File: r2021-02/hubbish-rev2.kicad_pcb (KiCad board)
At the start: 4 copper layers, 103.6 x 71.8 mm, 100 parts, among them J1 Conn_01x06, J10 USB_A_DUAL, J4 USB_A (female down), J5 Conn_01x03_Male, J6 USB_A_DUAL, J7 USB_A_DUAL, J8 USB_A male UP, J9 USB_B_Micro (up), U1 2k i2c eeprom, U10 NUP4202, U11 NUP4202, U12 NUP4202, U13 NUP4202, U14 NUP4202, U15 NUP4202, U16 NUP4202, U17 NUP4202, U18 SY8366H, U2 SE5120ST33, U3 USB2517, U4 APL3511C, U5 APL3511C, U6 APL3511C, U7 APL3511C, U8 APL3511C, U9 APL3511C, Y1 24MHz

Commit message: start rev2
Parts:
- removed C31: 100uF, Capacitor_SMD:CP_Elec_5x5.4
- removed J10, J7: USB_A_DUAL, Connector_USB:USB_A_Wuerth_61400826021_Horizontal_Stacked
- added C36: 10uF/50V, Capacitor_SMD:C_0805_2012Metric, F.Cu at (118.9, 61.7)
- added C37: 2.2uF, Capacitor_SMD:C_0603_1608Metric, F.Cu at (132.0, 65.0)
- added C38: 100nF, Capacitor_SMD:C_0603_1608Metric, F.Cu at (139.0, 108.5)
- added C39: Cff, Capacitor_SMD:C_0603_1608Metric, F.Cu at (135.9, 119.0)
- added C40: 22uF/6.3V, Capacitor_SMD:C_0805_2012Metric, F.Cu at (116.5, 72.6)
- added C41: 22uF/6.3V, Capacitor_SMD:C_0805_2012Metric, F.Cu at (120.5, 66.1)
- added C42: 22uF/6.3V, Capacitor_SMD:C_0805_2012Metric, F.Cu at (112.0, 72.6)
- added C43: 100uF, Capacitor_SMD:CP_Elec_5x5.4, F.Cu at (86.4, 144.6)
- added D12: SMF24A, Diode_SMD:D_SOD-123F, F.Cu at (106.2, 77.0)
- added D13: MBR1040, Package_TO_SOT_SMD:TO-252-2_TabPin1, F.Cu at (90.4, 65.3)
- added J2: USB_A_Stacked, Connector_USB:USB_A_Wuerth_61400826021_Horizontal_Stacked, F.Cu at (154.4, 140.2)
- added J3: USB_A_Stacked, Connector_USB:USB_A_Wuerth_61400826021_Horizontal_Stacked, F.Cu at (126.6, 142.7)
- added L1: 2.2uH, Inductor_SMD:L_CHILISIN_BMRx00060630, F.Cu at (108.8, 66.0)
- added R23: Rff, Resistor_SMD:R_0603_1608Metric, F.Cu at (125.7, 71.4)
- added R24: 100k/1%, Resistor_SMD:R_0603_1608Metric, F.Cu at (121.1, 73.4)
- added R25: 13k6/1%, Resistor_SMD:R_0603_1608Metric, F.Cu at (120.8, 77.1)
- added U19: APL3511C, Package_TO_SOT_SMD:SOT-23-5, F.Cu at (168.7, 114.1)
- C1: value 100uF -> 1uF; footprint Capacitor_SMD:CP_Elec_5x5.4 -> Capacitor_SMD:C_0603_1608Metric
- D1: value SD05-7 -> DF2S6.2FS,L3M; footprint Diode_SMD:D_SOD-323 -> Diode_SMD:D_SOD-923
- D9: value D_Small -> SM400x; footprint Diode_SMD:D_SOD-323 -> Diode_SMD:D_SOD-123F
- J6: value USB_A_DUAL -> USB_A_Stacked
- JP1: value Jumper_NO_Small -> Jumper_2_Open; footprint Connector_PinHeader_2.54mm:PinHeader_1x02_P2.54mm_Vertical -> TestPoint:TestPoint_2Pads_Pitch2.54mm_Drill0.8mm
- moved R21 145.9 mm to (179.9, 180.0), turned to 0 degrees
- moved R19 106.9 mm to (202.1, 162.6), turned to 0 degrees
- moved R10 104.4 mm to (205.0, 155.7), turned to 0 degrees
- moved D10 96.4 mm to (196.8, 152.5)
- moved D11 92.9 mm to (170.5, 180.7), turned to 0 degrees
- moved R15 92.1 mm to (209.0, 155.7), turned to 0 degrees
- moved R6 88.0 mm to (118.7, 131.5), turned to 0 degrees
- moved H2 86.4 mm to (178.2, 59.3)
- moved R4 84.7 mm to (126.7, 130.9)
- moved D3 82.8 mm to (175.0, 79.0), turned to 0 degrees
- moved D2 82.7 mm to (175.3, 75.9), turned to 0 degrees
- moved R20 81.3 mm to (180.3, 172.9), turned to 0 degrees
- moved C33 76.9 mm to (131.9, 121.5)
- moved D8 76.9 mm to (180.7, 169.3)
- moved H1 73.2 mm to (178.2, 52.3)
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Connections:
- C19 pad 1: +5V -> /downstream-port-power/VBUS_DS
- J1 pad 6: (no net) -> Net-(D13-Pad2)
- J4 pad 1: +5V -> /downstream-port-power/VBUS_DS
- J5 pad 2: /upstream-config-leds/CFG_SEL0 -> /upstream-config-leds/EE_SCL
- J6 pad 1: /downstream-port-power/VBUS3 -> /downstream-port-power/VBUS5
- J6 pad 2: /downstream-port-power/U3- -> /downstream-port-power/U5-
- J6 pad 3: /downstream-port-power/U3+ -> /downstream-port-power/U5+
- J6 pad 5: /downstream-port-power/VBUS4 -> /downstream-port-power/VBUS6
- J6 pad 6: /downstream-port-power/U4- -> /downstream-port-power/U6-
- J6 pad 7: /downstream-port-power/U4+ -> /downstream-port-power/U6+
- R7 pad 2: /upstream-config-leds/CFG_SEL0 -> /upstream-config-leds/CFG_SEL0-EE_SCL
- R8 pad 1: /upstream-config-leds/CFG_SEL0 -> /upstream-config-leds/CFG_SEL0-EE_SCL
- U1 pad 6: /upstream-config-leds/CFG_SEL0 -> /upstream-config-leds/EE_SCL
- U10 pad 3: unconnected-(U10-Pad3) -> (no net)
- U10 pad 4: unconnected-(U10-Pad4) -> (no net)
- U11 pad 3: unconnected-(U11-Pad3) -> (no net)
- U11 pad 4: unconnected-(U11-Pad4) -> (no net)
- U12 pad 1: unconnected-(U12-Pad1) -> (no net)
- U12 pad 6: unconnected-(U12-Pad6) -> (no net)
- U13 pad 3: unconnected-(U13-Pad3) -> (no net)
- U13 pad 4: unconnected-(U13-Pad4) -> (no net)
- U14 pad 1: unconnected-(U14-Pad1) -> (no net)
- U14 pad 6: unconnected-(U14-Pad6) -> (no net)
- U15 pad 1: unconnected-(U15-Pad1) -> (no net)
- U15 pad 6: unconnected-(U15-Pad6) -> (no net)
- U16 pad 1: unconnected-(U16-Pad1) -> (no net)
- U16 pad 6: unconnected-(U16-Pad6) -> (no net)
- U17 pad 1: unconnected-(U17-Pad1) -> (no net)
- U17 pad 6: unconnected-(U17-Pad6) -> (no net)
- U18 pad 1: unconnected-(U18-Pad1) -> GND
- U18 pad 10: unconnected-(U18-Pad10) -> (no net)
- U18 pad 11: unconnected-(U18-Pad11) -> (no net)
- U18 pad 12: unconnected-(U18-Pad12) -> +VDC
- U18 pad 2: unconnected-(U18-Pad2) -> Net-(C38-Pad2)
- U18 pad 5: (no net) -> +VDC
- U18 pad 6: (no net) -> +VDC
- U18 pad 7: unconnected-(U18-Pad7) -> Net-(C38-Pad1)
- U18 pad 8: unconnected-(U18-Pad8) -> Net-(C37-Pad1)
- U18 pad 9: unconnected-(U18-Pad9) -> Net-(R23-Pad1)
- U3 pad 14: unconnected-(U3-Pad14) -> (no net)
- U3 pad 16: unconnected-(U3-Pad16) -> (no net)
- U3 pad 18: unconnected-(U3-Pad18) -> (no net)
- U3 pad 30: unconnected-(U3-Pad30) -> /downstream-port-power/EN_DS
- U3 pad 32: unconnected-(U3-Pad32) -> (no net)
- U3 pad 34: unconnected-(U3-Pad34) -> (no net)
- U3 pad 35: unconnected-(U3-Pad35) -> /downstream-port-power/OC_DS
- U3 pad 41: /upstream-config-leds/CFG_SEL0 -> /upstream-config-leds/CFG_SEL0-EE_SCL
- U3 pad 48: unconnected-(U3-Pad48) -> (no net)
- U3 pad 50: unconnected-(U3-Pad50) -> (no net)
- U3 pad 60: Net-(C4-Pad1) -> (no net)
- U3 pad 61: Net-(C5-Pad2) -> (no net)
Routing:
- net GNDPWR: track 306.4 -> 0.00 mm, vias 1 -> 0
- net +3V3: track 109.4 -> 0.00 mm, vias 27 -> 0
- net /upstream-config-leds/CFG_SEL1: track 98.5 -> 0.00 mm
- net /downstream-port-power/EN5: track 89.0 -> 0.00 mm, vias 2 -> 0
- net /downstream-port-power/OC5: track 87.8 -> 0.00 mm, vias 2 -> 0
- net /upstream-config-leds/UP-: track 85.4 -> 0.00 mm, vias 2 -> 0
- net /upstream-config-leds/UP+: track 84.4 -> 0.00 mm, vias 2 -> 0
- net GND: track 77.4 -> 0.00 mm, vias 59 -> 0
- net /upstream-config-leds/LED_A3: track 75.7 -> 0.00 mm, vias 2 -> 0
- net /upstream-config-leds/LED_A6: track 75.4 -> 0.00 mm, vias 2 -> 0
- net /downstream-port-power/EN6: track 73.6 -> 0.00 mm, vias 2 -> 0
- net /upstream-config-leds/LED_A1: track 72.6 -> 0.00 mm, vias 4 -> 0
- net /downstream-port-power/OC6: track 69.9 -> 0.00 mm, vias 2 -> 0
- net /upstream-config-leds/LED_A7: track 68.5 -> 0.00 mm, vias 2 -> 0
- net /downstream-port-power/EN3: track 67.5 -> 0.00 mm, vias 2 -> 0
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- removed copper zone on F.Cu, net +3V3
- removed copper zone on In2.Cu, net +3V3
- removed copper zone on In2.Cu, net +5V
- removed copper zone on B.Cu, net /upstream-config-leds/LED_DRIVE
- removed copper zone on F.Cu, net GND
- removed copper zone on In1.Cu, net GND
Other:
- board size 103.6 x 71.8 mm -> 100 x 100 mm
- copper layers 4 -> 2
- board text removed: "+5V"
- board text removed: "0"
- board text removed: "1"
- board text removed: "2"
- board text removed: "BIG fatto 30W 5V supply here one day y0"
- board text removed: "CFG_SEL"
- board text removed: "GND"
- board text removed: "GND SCL SDA"
- board text removed: "HI"
- board text removed: "HiSpeed"
- board text removed: "JLCJLCJLCJLC"
- board text removed: "JLCPCB 2313 stackup!"
- board text removed: "LO"
- board text removed: "Port 1/2"
- board text removed: "Port 3/4"
- board text removed: "Port 5"
- board text removed: "Port 6/7"
- board text removed: "Port LEDs Green: LS Red: FS Orange: HS"
- board text removed: "Reset"
- board text removed: "Upstream"
- board text removed: "github.com/karlp/hubbish rev 2020-03"

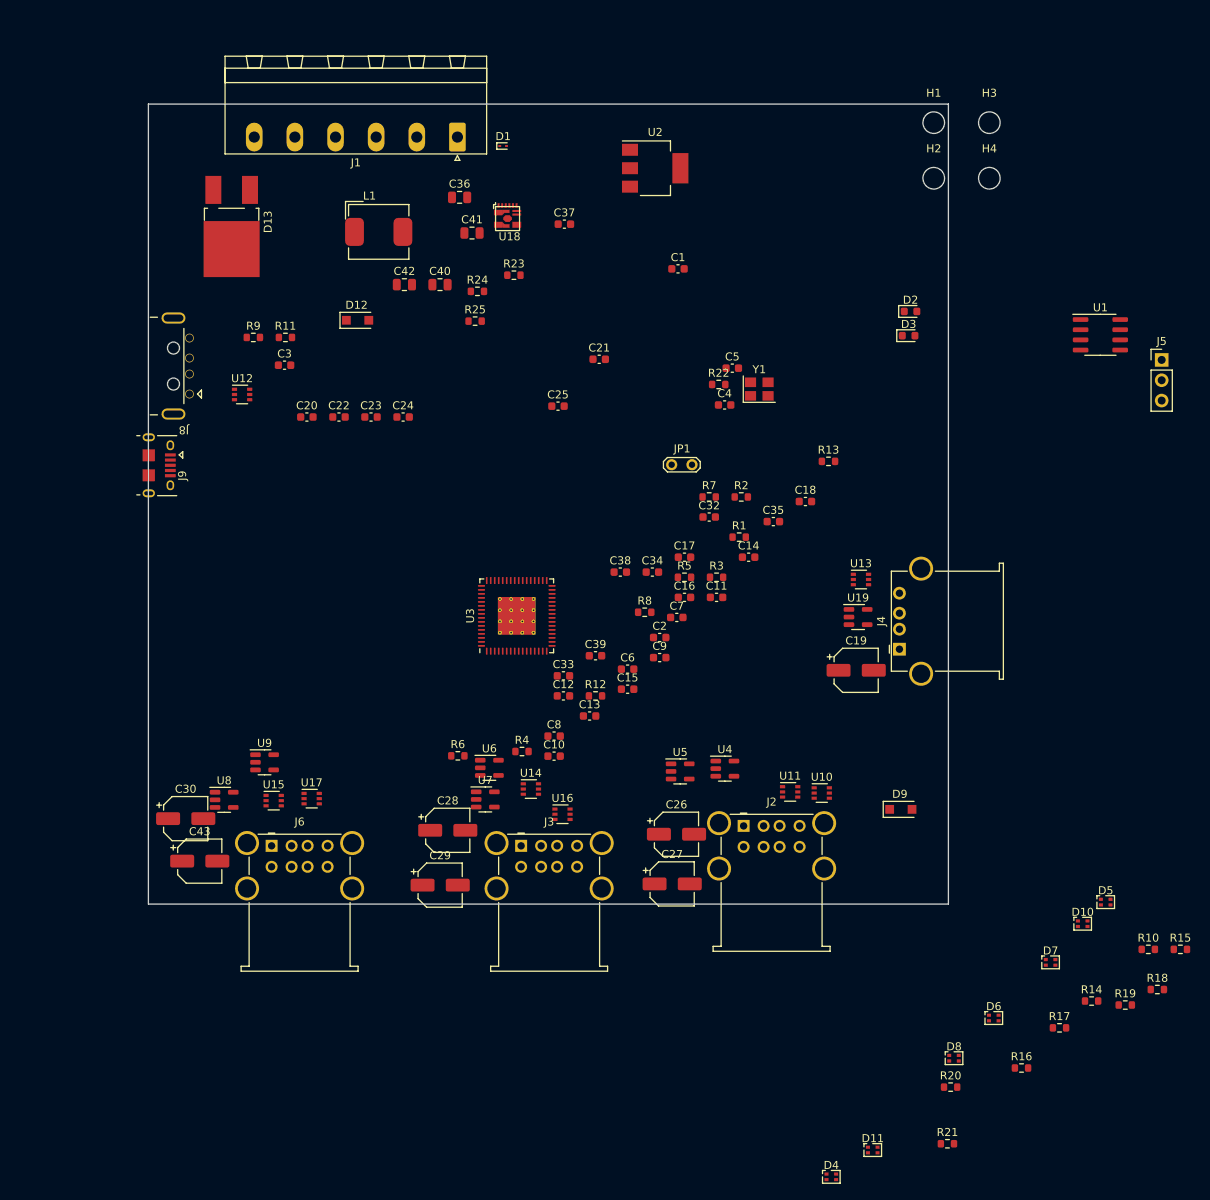
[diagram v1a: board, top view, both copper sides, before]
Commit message: rev2: start pcb work.
Looks like lots of space on a 100mm square...
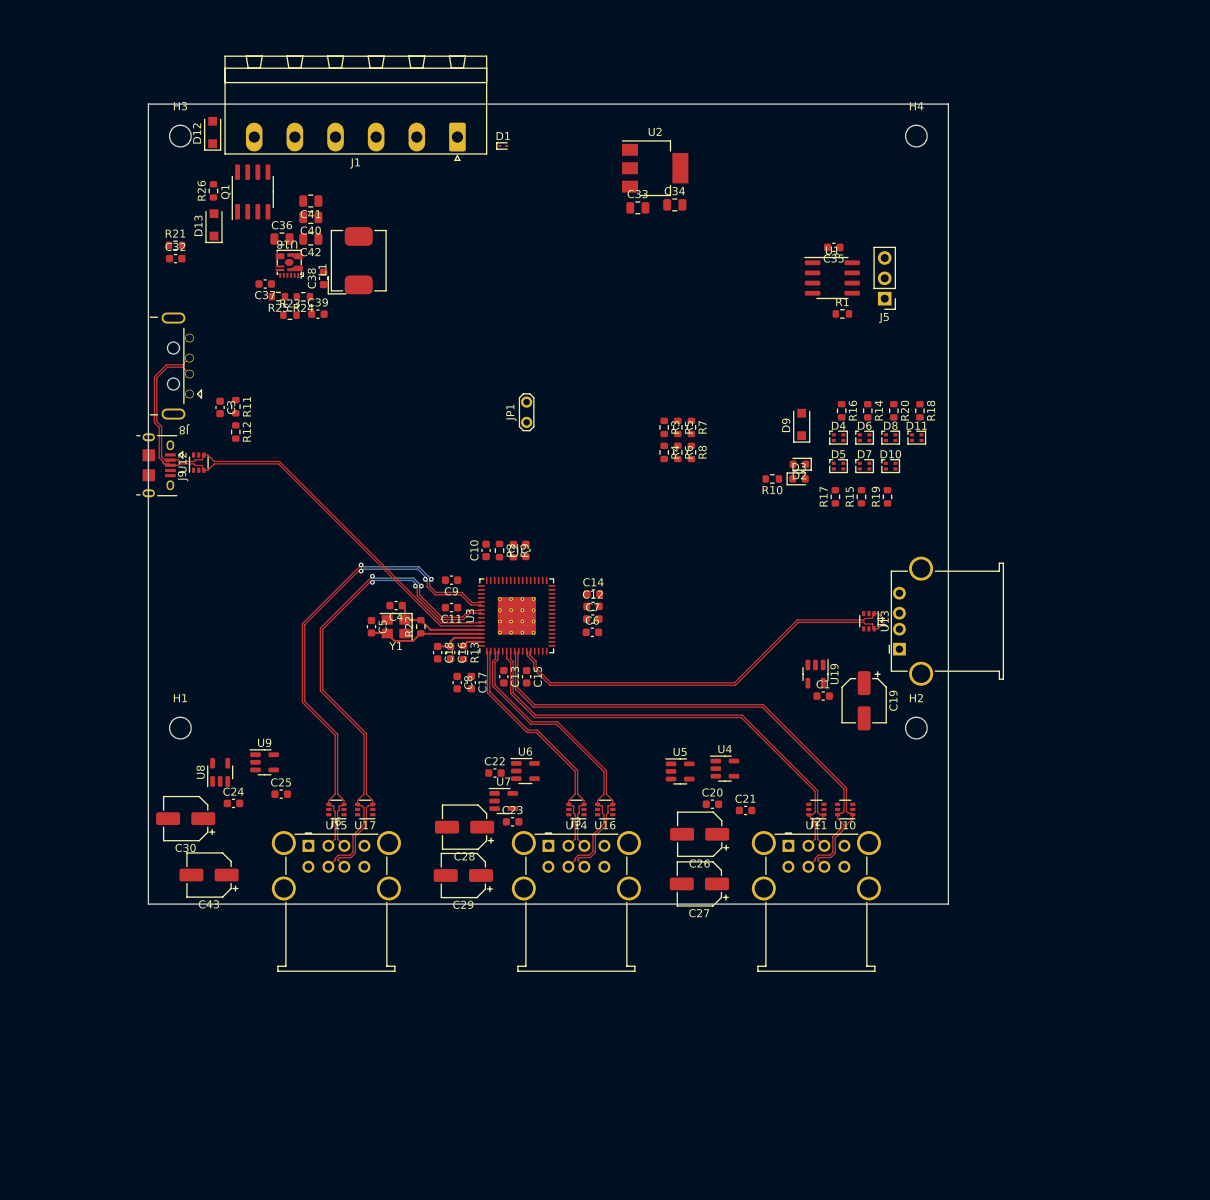
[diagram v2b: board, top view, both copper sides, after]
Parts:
- added Q1: Si4435, Package_SO:SOIC-8_3.9x4.9mm_P1.27mm, F.Cu at (93.0, 61.0)
- added R26: 330, Resistor_SMD:R_0603_1608Metric, F.Cu at (88.1, 60.9)
- C33, C34: footprint Capacitor_SMD:C_0603_1608Metric -> Capacitor_SMD:C_0805_2012Metric
- D13: value MBR1040 -> 6.8V Zener or so; footprint Package_TO_SOT_SMD:TO-252-2_TabPin1 -> Diode_SMD:D_SOD-123F
- moved R21 148.1 mm to (83.4, 67.7)
- moved H1 120.8 mm to (84.0, 128.0)
- moved H3 101.1 mm to (84.0, 54.0)
- moved D4 92.4 mm to (166.3, 91.7)
- moved D11 89.2 mm to (176.0, 91.7)
- moved R16 85.2 mm to (166.7, 88.3), turned to -90 degrees
- moved R20 84.8 mm to (173.2, 88.3), turned to -90 degrees
- moved R14 78.9 mm to (169.9, 88.3), turned to -90 degrees
- moved R18 78.2 mm to (176.4, 88.3), turned to -90 degrees
- moved D8 78.0 mm to (172.8, 91.7)
- moved R10 75.3 mm to (158.0, 96.9), turned to 180 degrees
- moved D6 74.3 mm to (169.5, 91.7)
- moved C32 74.1 mm to (83.4, 69.3)
- moved R17 72.1 mm to (165.9, 99.1), turned to 90 degrees
- moved R19 70.1 mm to (172.4, 99.1), turned to 90 degrees
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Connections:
- net Net-(C37-Pad1) renamed /upstream-config-leds/SY-VCC
- net Net-(C38-Pad1) renamed /upstream-config-leds/BST
- net Net-(C38-Pad2) renamed /upstream-config-leds/LX
- net Net-(R23-Pad1) renamed /upstream-config-leds/SY-FB
- C4 pad 1: Net-(C4-Pad1) -> /upstream-config-leds/xtal2
- C5 pad 2: Net-(C5-Pad2) -> /upstream-config-leds/xtal1
- D12 pad 1: +VDC -> /upstream-config-leds/PWR_RAW
- J1 pad 6: Net-(D13-Pad2) -> /upstream-config-leds/PWR_RAW
- R22 pad 1: Net-(C5-Pad2) -> /upstream-config-leds/xtal1
- R22 pad 2: Net-(C4-Pad1) -> /upstream-config-leds/xtal2
- U3 pad 60: (no net) -> /upstream-config-leds/xtal2
- U3 pad 61: (no net) -> /upstream-config-leds/xtal1
- Y1 pad 1: Net-(C4-Pad1) -> /upstream-config-leds/xtal2
- Y1 pad 3: Net-(C5-Pad2) -> /upstream-config-leds/xtal1
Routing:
- net /upstream-config-leds/UP+: track 0.00 -> 65.9 mm
- net /upstream-config-leds/UP-: track 0.00 -> 64.9 mm
- net /downstream-port-power/U2-: track 0.00 -> 64.4 mm
- net /downstream-port-power/U2+: track 0.00 -> 64.4 mm
- net /downstream-port-power/U6-: track 0.00 -> 62.0 mm, vias 0 -> 2
- net /downstream-port-power/U6+: track 0.00 -> 61.2 mm, vias 0 -> 2
- net /downstream-port-power/U5-: track 0.00 -> 59.0 mm, vias 0 -> 2
- net /downstream-port-power/U5+: track 0.00 -> 58.1 mm, vias 0 -> 2
- net /downstream-port-power/U1-: track 0.00 -> 56.7 mm
- net /downstream-port-power/U1+: track 0.00 -> 56.7 mm
- net /downstream-port-power/DS-: track 0.00 -> 51.5 mm
- net /downstream-port-power/DS+: track 0.00 -> 51.0 mm
- net /downstream-port-power/U4-: track 0.00 -> 38.4 mm
- net /downstream-port-power/U4+: track 0.00 -> 38.4 mm
- net /downstream-port-power/U3-: track 0.00 -> 30.9 mm
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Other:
- copper layers 2 -> 4

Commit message: hubbish 2021-2 updates
line it up a bit better, realise parts are no longer available, start
kidding myself I'm working on this again.
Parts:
- added R27: 100k, Resistor_SMD:R_0603_1608Metric, F.Cu at (91.6, 70.2)
- added R28: 100k, Resistor_SMD:R_0603_1608Metric, F.Cu at (87.6, 70.2)
- moved R21 58.8 mm to (88.9, 126.2), turned to 180 degrees
- moved C32 55.5 mm to (88.9, 124.6), turned to 180 degrees
- moved C24 51.1 mm to (141.7, 138.8), turned to 90 degrees
- moved U5 28.7 mm to (174.7, 138.6), turned to 180 degrees
- moved C43 28.3 mm to (115.8, 144.7), turned to -90 degrees
- moved R10 27.9 mm to (130.3, 99.7), turned to -90 degrees
- moved C27 27.1 mm to (175.8, 144.7), turned to -90 degrees
- moved C29 26.5 mm to (145.8, 144.7), turned to -90 degrees
- moved J9 24.9 mm to (81.6, 120.0)
- moved U12 24.9 mm to (87.8, 119.7)
- moved C3 24.6 mm to (88.9, 112.5)
- moved J8 24.6 mm to (83.1, 107.3)
- moved R11 24.6 mm to (90.9, 112.4)
- moved R12 24.6 mm to (90.9, 115.5)
- moved U9 21.1 mm to (114.7, 138.6), turned to 180 degrees
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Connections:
- net /upstream-config-leds/~RESET renamed /upstream-config-leds/~{RESET}
- net Net-(D13-Pad2) renamed /upstream-config-leds/PolProtG
- J9 pad 4: (no net) -> unconnected-(J9-Pad4)
- U10 pad 1: /downstream-port-power/U2+ -> unconnected-(U10-Pad1)
- U10 pad 3: (no net) -> /downstream-port-power/U2-
- U10 pad 4: (no net) -> /downstream-port-power/U2+
- U10 pad 6: /downstream-port-power/U2- -> unconnected-(U10-Pad6)
- U11 pad 3: (no net) -> unconnected-(U11-Pad3)
- U11 pad 4: (no net) -> unconnected-(U11-Pad4)
- U12 pad 1: (no net) -> unconnected-(U12-Pad1)
- U12 pad 6: (no net) -> unconnected-(U12-Pad6)
- U13 pad 3: (no net) -> unconnected-(U13-Pad3)
- U13 pad 4: (no net) -> unconnected-(U13-Pad4)
- U13 pad 5: +5V -> /downstream-port-power/VBUS_DS
- U14 pad 1: (no net) -> /downstream-port-power/U3+
- U14 pad 3: /downstream-port-power/U3+ -> unconnected-(U14-Pad3)
- U14 pad 4: /downstream-port-power/U3- -> unconnected-(U14-Pad4)
- U14 pad 6: (no net) -> /downstream-port-power/U3-
- U15 pad 1: (no net) -> /downstream-port-power/U5+
- U15 pad 3: /downstream-port-power/U5+ -> unconnected-(U15-Pad3)
- U15 pad 4: /downstream-port-power/U5- -> unconnected-(U15-Pad4)
- U15 pad 6: (no net) -> /downstream-port-power/U5-
- U16 pad 1: (no net) -> unconnected-(U16-Pad1)
- U16 pad 3: /downstream-port-power/U4+ -> /downstream-port-power/U4-
- U16 pad 4: /downstream-port-power/U4- -> /downstream-port-power/U4+
- U16 pad 6: (no net) -> unconnected-(U16-Pad6)
- U17 pad 1: (no net) -> unconnected-(U17-Pad1)
- U17 pad 3: /downstream-port-power/U6+ -> /downstream-port-power/U6-
- U17 pad 4: /downstream-port-power/U6- -> /downstream-port-power/U6+
- U17 pad 6: (no net) -> unconnected-(U17-Pad6)
- U18 pad 10: (no net) -> Net-(R27-Pad2)
- U18 pad 11: (no net) -> unconnected-(U18-Pad11)
- U18 pad 3: (no net) -> unconnected-(U18-Pad3)
- U18 pad 4: (no net) -> unconnected-(U18-Pad4)
- U3 pad 14: (no net) -> unconnected-(U3-Pad14)
- U3 pad 16: (no net) -> unconnected-(U3-Pad16)
- U3 pad 18: (no net) -> unconnected-(U3-Pad18)
- U3 pad 32: (no net) -> unconnected-(U3-Pad32)
- U3 pad 34: (no net) -> unconnected-(U3-Pad34)
- U3 pad 48: (no net) -> unconnected-(U3-Pad48)
- U3 pad 50: (no net) -> unconnected-(U3-Pad50)
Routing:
- net GNDPWR: track 0.00 -> 232.5 mm
- net GND: track 0.00 -> 86.7 mm, vias 0 -> 26
- net +5V: track 0.00 -> 43.9 mm, vias 0 -> 7
- net /upstream-config-leds/CFG_SEL1: track 0.00 -> 35.1 mm
- net +3V3: track 0.00 -> 33.2 mm, vias 0 -> 8
- net /downstream-port-power/VBUS4: track 0.00 -> 31.1 mm
- net /downstream-port-power/VBUS2: track 0.00 -> 29.6 mm
- net /downstream-port-power/VBUS6: track 0.00 -> 29.1 mm
- net /downstream-port-power/VBUS5: track 0.00 -> 18.1 mm
- net /downstream-port-power/VBUS1: track 0.00 -> 18.1 mm
- net /downstream-port-power/VBUS3: track 0.00 -> 17.7 mm
- net /upstream-config-leds/CFG_SEL0-EE_SCL: track 0.00 -> 13.1 mm
- net /downstream-port-power/VBUS_DS: track 0.00 -> 11.5 mm
- net /upstream-config-leds/CFG_SEL1_A: track 0.00 -> 11.4 mm
- net /upstream-config-leds/PolProtG: track 0.00 -> 11.1 mm
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- added copper zone on In2.Cu, net +5V
- added copper zone on F.Cu, net /upstream-config-leds/PWR_RAW
- added copper zone on In1.Cu, net GND
